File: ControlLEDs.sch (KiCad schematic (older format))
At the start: 18 parts

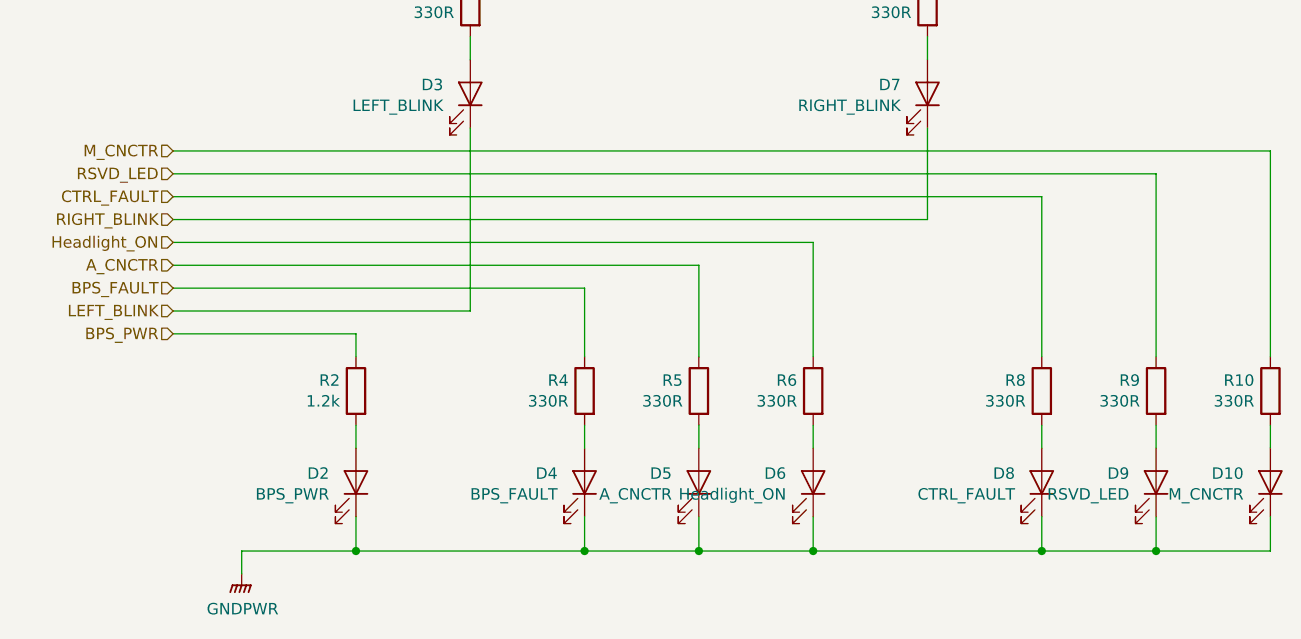
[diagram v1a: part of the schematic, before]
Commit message: Added Regen switch, deleted RSVD LED
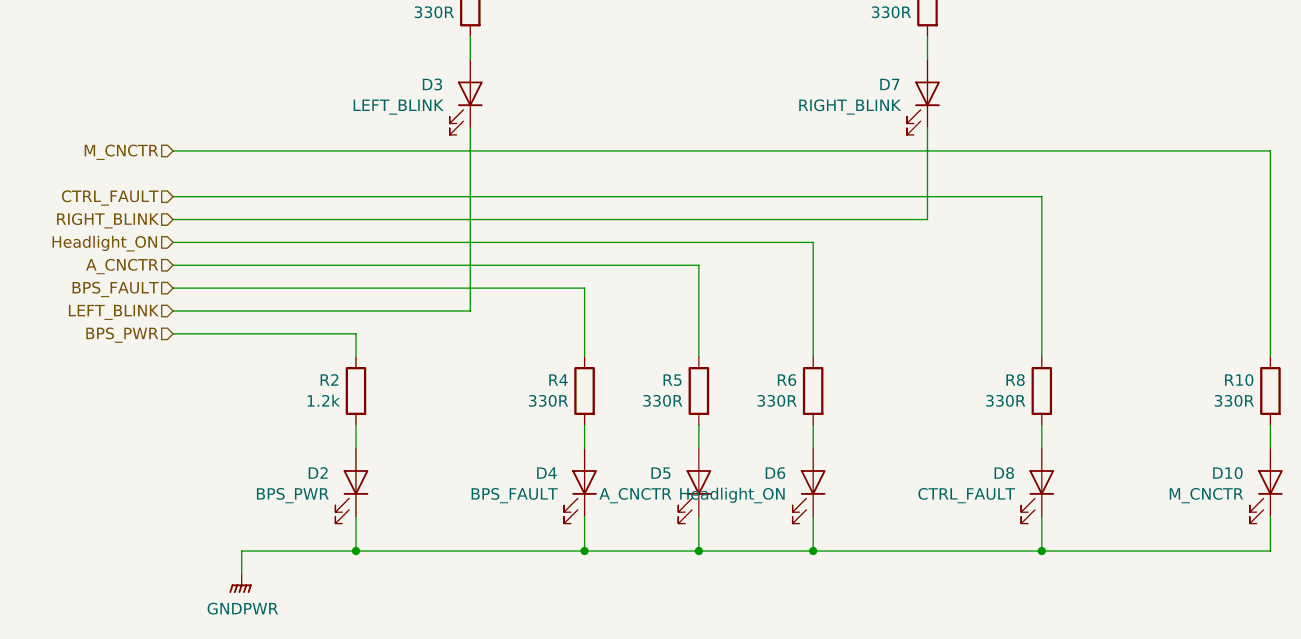
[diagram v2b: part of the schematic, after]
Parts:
- removed D9: RSVD_LED, Diode_SMD:D_0805_2012Metric, symbol Device:LED
- removed R9: 330R, Resistor_SMD:R_0805_2012Metric, symbol Device:R
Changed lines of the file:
@@
 $EndComp
-Wire Wire Line
-	7900 4250 7900 4350
 Wire Wire Line
 	7400 4250 7400 4350
@@
 Wire Wire Line
 	7400 3250 7400 3950
-Wire Wire Line
-	3600 3150 7900 3150
-Wire Wire Line
-	7900 3150 7900 3950
 Wire Wire Line
 	3600 3050 8400 3050
@@
 Wire Wire Line
 	7400 4650 7400 4800
-Wire Wire Line
-	7900 4650 7900 4800
-Wire Wire Line
-	7900 4800 7400 4800
 Connection ~ 7400 4800
 Wire Wire Line
 	8400 4650 8400 4800
-Wire Wire Line
-	8400 4800 7900 4800
-Connection ~ 7900 4800
 Wire Wire Line
 	3900 2150 3900 2050
@@
 Text HLabel 3600 3050 0    50   Input ~ 0
 M_CNCTR
-Text HLabel 3600 3150 0    50   Input ~ 0
-RSVD_LED
 Text HLabel 3600 3450 0    50   Input ~ 0
 Headlight_ON
@@
 $Comp
 L Device:R R?
-U 1 1 5F7BCB8B
-P 7900 4100
-AR Path="/5F7BCB8B" Ref="R?"  Part="1"
-AR Path="/5F7A71E1/5F7BCB8B" Ref="R9"  Part="1"
-F 0 "R9" H 7970 4146 50  0000 L CNN
-F 1 "330R" H 7970 4055 50  0000 L CNN
-F 2 "Resistor_SMD:R_0805_2012Metric" V 7830 4100 50  0001 C CNN
-F 3 "~" H 7900 4100 50  0001 C CNN
-	1    7900 4100
-	-1   0    0    -1
-$EndComp
-$Comp
-L Device:R R?
 U 1 1 5F7BCB85
 P 7400 4100
@@
 $EndComp
 $Comp
-L Device:LED D?
-U 1 1 5F7BCB61
-P 7900 4500
-AR Path="/5F7BCB61" Ref="D?"  Part="1"
-AR Path="/5F7A71E1/5F7BCB61" Ref="D9"  Part="1"
-F 0 "D9" V 7939 4383 50  0000 R CNN
-F 1 "RSVD_LED" V 7848 4383 50  0000 R CNN
-F 2 "Diode_SMD:D_0805_2012Metric" H 7900 4500 50  0001 C CNN
-F 3 "~" H 7900 4500 50  0001 C CNN
-	1    7900 4500
-	0    1    -1   0
-$EndComp
-$Comp
 L Device:R R?
 U 1 1 5F7BCB9D
@@
 	-1   0    0    -1
 $EndComp
+Wire Wire Line
+	7400 4800 8400 4800
 $EndSCHEMATC

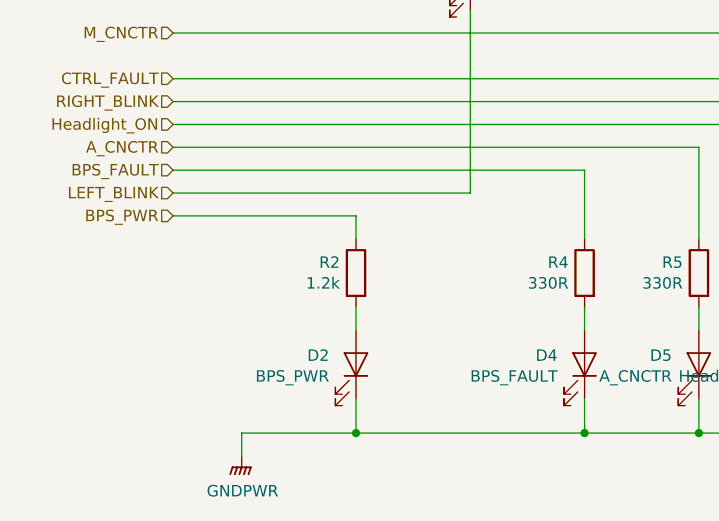
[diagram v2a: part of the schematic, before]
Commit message: Fixed BPS_PWR lines
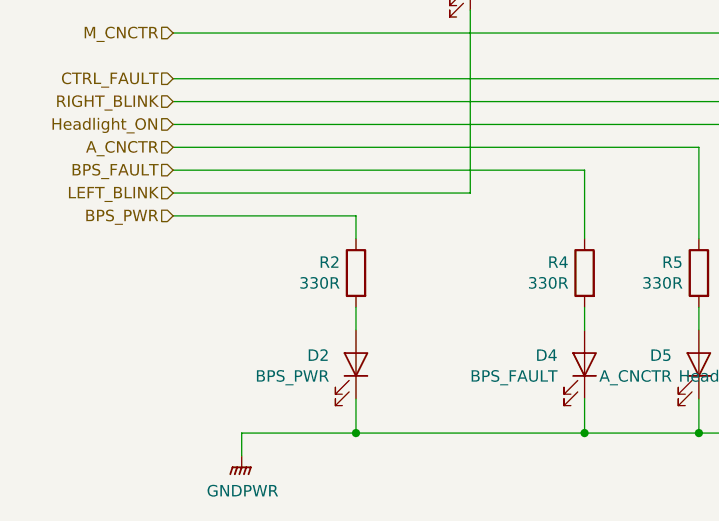
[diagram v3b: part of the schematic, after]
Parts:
- R2: value 1.2k -> 330R
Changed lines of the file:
@@
 AR Path="/5F7A71E1/5F7BCBA3" Ref="R2"  Part="1"
 F 0 "R2" H 4470 4146 50  0000 L CNN
-F 1 "1.2k" H 4470 4055 50  0000 L CNN
+F 1 "330R" H 4470 4055 50  0000 L CNN
 F 2 "Resistor_SMD:R_0805_2012Metric" V 4330 4100 50  0001 C CNN
 F 3 "~" H 4400 4100 50  0001 C CNN

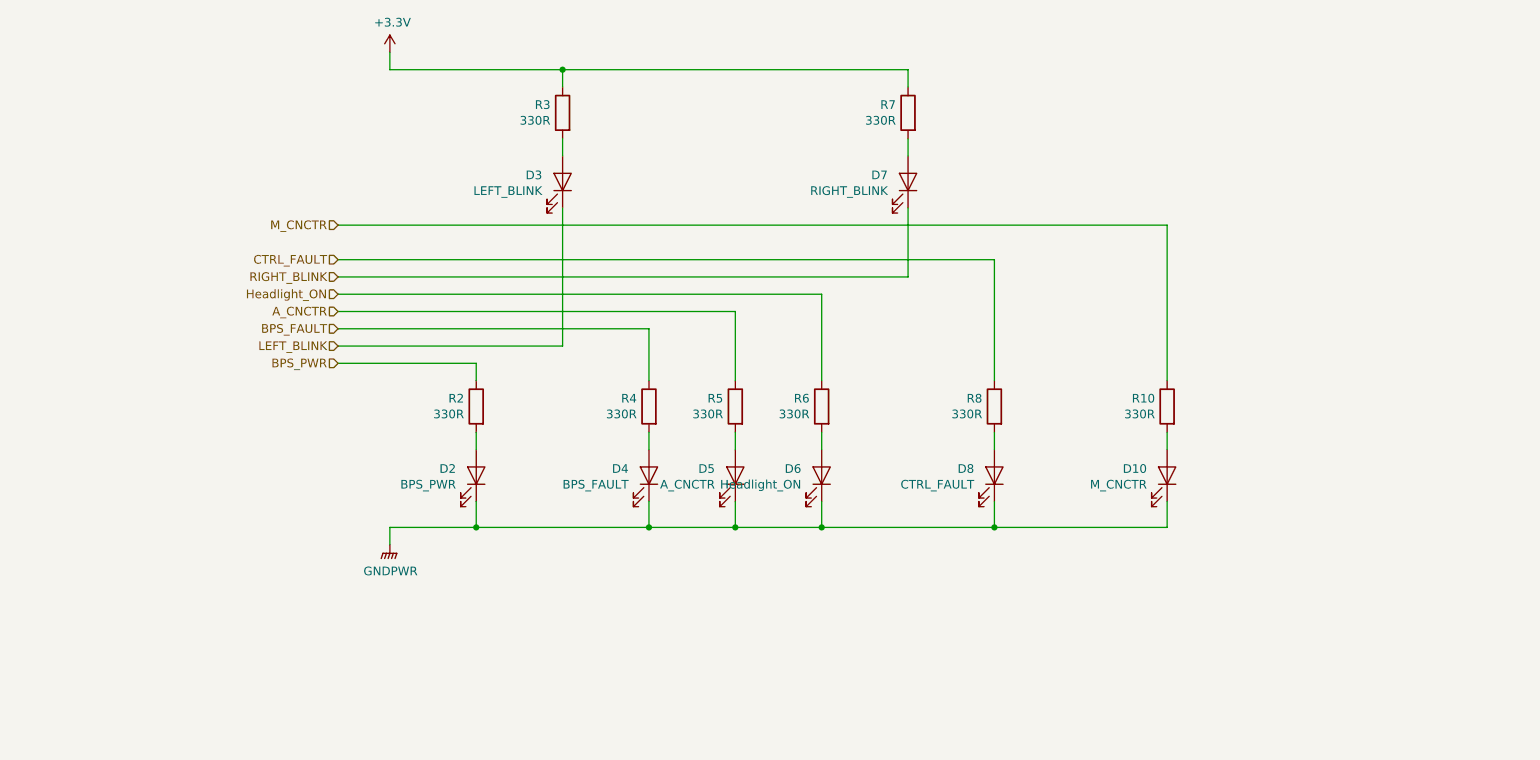
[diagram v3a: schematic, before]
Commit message: Changed Schematic, but not PCB layout. Updated LED resistor values
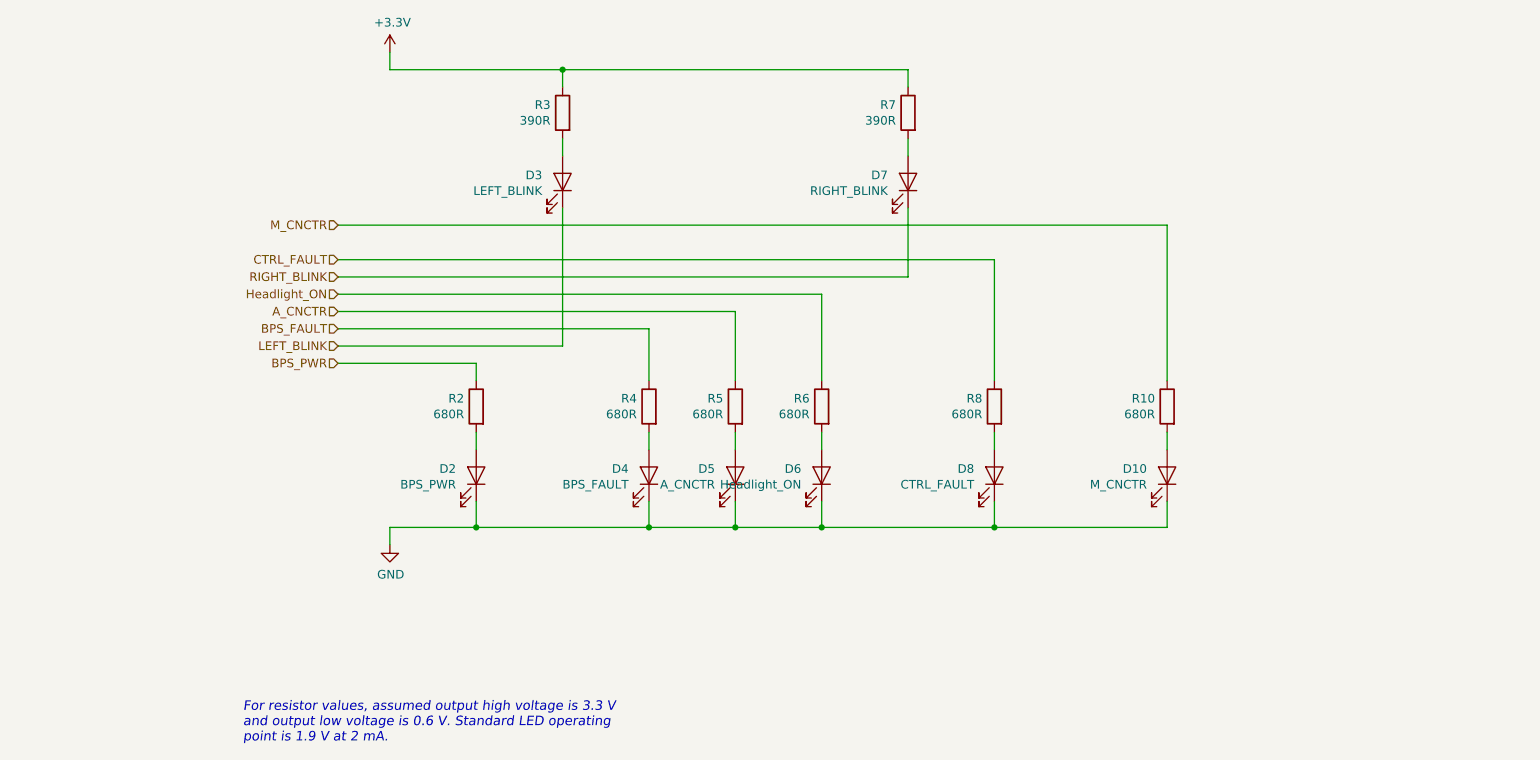
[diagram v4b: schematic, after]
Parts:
- R10, R2, R4, R5, R6, R8: value 330R -> 680R
- R3, R7: value 330R -> 390R
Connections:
- net GNDPWR renamed GND
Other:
- note added: "For resistor values, assumed output high voltage is 3.3 V \nand output low voltage is 0.6 V. Standard LED operating \npoint is 1.9 V at 2 mA."
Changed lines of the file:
@@
 $Descr A4 11693 8268
 encoding utf-8
-Sheet 2 5
+Sheet 3 4
 Title ""
 Date ""
@@
 AR Path="/5F7A71E1/5F7BCB91" Ref="R6"  Part="1"
 F 0 "R6" H 6470 4146 50  0000 L CNN
-F 1 "330R" H 6470 4055 50  0000 L CNN
+F 1 "680R" H 6470 4055 50  0000 L CNN
 F 2 "Resistor_SMD:R_0805_2012Metric" V 6330 4100 50  0001 C CNN
 F 3 "~" H 6400 4100 50  0001 C CNN
@@
 AR Path="/5F7A71E1/5F7BCBA3" Ref="R2"  Part="1"
 F 0 "R2" H 4470 4146 50  0000 L CNN
-F 1 "330R" H 4470 4055 50  0000 L CNN
+F 1 "680R" H 4470 4055 50  0000 L CNN
 F 2 "Resistor_SMD:R_0805_2012Metric" V 4330 4100 50  0001 C CNN
 F 3 "~" H 4400 4100 50  0001 C CNN
@@
 AR Path="/5F7A71E1/5F7BCBA9" Ref="R3"  Part="1"
 F 0 "R3" H 4970 2446 50  0000 L CNN
-F 1 "330R" H 4970 2355 50  0000 L CNN
+F 1 "390R" H 4970 2355 50  0000 L CNN
 F 2 "Resistor_SMD:R_0805_2012Metric" V 4830 2400 50  0001 C CNN
 F 3 "~" H 4900 2400 50  0001 C CNN
@@
 AR Path="/5F7A71E1/5F7BCBAF" Ref="R4"  Part="1"
 F 0 "R4" H 5470 4146 50  0000 L CNN
-F 1 "330R" H 5470 4055 50  0000 L CNN
+F 1 "680R" H 5470 4055 50  0000 L CNN
 F 2 "Resistor_SMD:R_0805_2012Metric" V 5330 4100 50  0001 C CNN
 F 3 "~" H 5400 4100 50  0001 C CNN
@@
 F 3 "" H 3900 2050 50  0001 C CNN
 	1    3900 2050
-	1    0    0    -1
-$EndComp
-$Comp
-L power:GNDPWR #PWR?
-U 1 1 5F7BCBC1
-P 3900 4900
-AR Path="/5F7BCBC1" Ref="#PWR?"  Part="1"
-AR Path="/5F7A71E1/5F7BCBC1" Ref="#PWR0115"  Part="1"
-F 0 "#PWR0115" H 3900 4700 50  0001 C CNN
-F 1 "GNDPWR" H 3904 4746 50  0000 C CNN
-F 2 "" H 3900 4850 50  0001 C CNN
-F 3 "" H 3900 4850 50  0001 C CNN
-	1    3900 4900
 	1    0    0    -1
 $EndComp
@@
 AR Path="/5F7A71E1/5F7BCBD8" Ref="R10"  Part="1"
 F 0 "R10" H 8470 4146 50  0000 L CNN
-F 1 "330R" H 8470 4055 50  0000 L CNN
+F 1 "680R" H 8470 4055 50  0000 L CNN
 F 2 "Resistor_SMD:R_0805_2012Metric" V 8330 4100 50  0001 C CNN
 F 3 "~" H 8400 4100 50  0001 C CNN
@@
 AR Path="/5F7A71E1/5F7BCB85" Ref="R8"  Part="1"
 F 0 "R8" H 7470 4146 50  0000 L CNN
-F 1 "330R" H 7470 4055 50  0000 L CNN
+F 1 "680R" H 7470 4055 50  0000 L CNN
 F 2 "Resistor_SMD:R_0805_2012Metric" V 7330 4100 50  0001 C CNN
 F 3 "~" H 7400 4100 50  0001 C CNN
@@
 AR Path="/5F7A71E1/5F7BCB9D" Ref="R5"  Part="1"
 F 0 "R5" H 5970 4146 50  0000 L CNN
-F 1 "330R" H 5970 4055 50  0000 L CNN
+F 1 "680R" H 5970 4055 50  0000 L CNN
 F 2 "Resistor_SMD:R_0805_2012Metric" V 5830 4100 50  0001 C CNN
 F 3 "~" H 5900 4100 50  0001 C CNN
@@
 AR Path="/5F7A71E1/5F7BCB97" Ref="R7"  Part="1"
 F 0 "R7" H 6970 2446 50  0000 L CNN
-F 1 "330R" H 6970 2355 50  0000 L CNN
+F 1 "390R" H 6970 2355 50  0000 L CNN
 F 2 "Resistor_SMD:R_0805_2012Metric" V 6830 2400 50  0001 C CNN
 F 3 "~" H 6900 2400 50  0001 C CNN
@@
 Wire Wire Line
 	7400 4800 8400 4800
+$Comp
+L power:GND #PWR020
+U 1 1 5FDE5ADE
+P 3900 4900
+F 0 "#PWR020" H 3900 4650 50  0001 C CNN
+F 1 "GND" H 3905 4727 50  0000 C CNN
+F 2 "" H 3900 4900 50  0001 C CNN
+F 3 "" H 3900 4900 50  0001 C CNN
+	1    3900 4900
+	1    0    0    -1
+$EndComp
+Text Notes 3050 6050 0    55   Italic 0
+For resistor values, assumed output high voltage is 3.3 V \nand output low voltage is 0.6 V. Standard LED operating \npoint is 1.9 V at 2 mA.
 $EndSCHEMATC

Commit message: Board finished with the new changes, needs to be checked
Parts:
- R10, R2, R5, R6, R8: value 680R -> 680
- R3, R7: value 390R -> 390
- R4: value 680R -> 5k
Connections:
- net GND: no longer D4.1 (K)
- net BPS_FAULT renamed BPS_FAULT+
- new net BPS_FAULT-: D4.1 (K)
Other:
- note added: "For all resistor values (other than BPS_FAULT), the assumed output high voltage is 3.3 V \nand output low voltage is 0.6 V. Standard LED operating point is 1.9 V at 2 mA."
- note added: "Voltage drop from BPS_FAULT+ to BPS_FAULT- \nis assumed to be 12 V."
- note removed: "For resistor values, assumed output high voltage is 3.3 V \nand output low voltage is 0.6 V. Standard LED operating \npoint is 1.9 V at 2 mA."
- moved on the sheet: D10, D2, D3, D4, D5, D6, D7, D8, R10, R2, R3, R4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

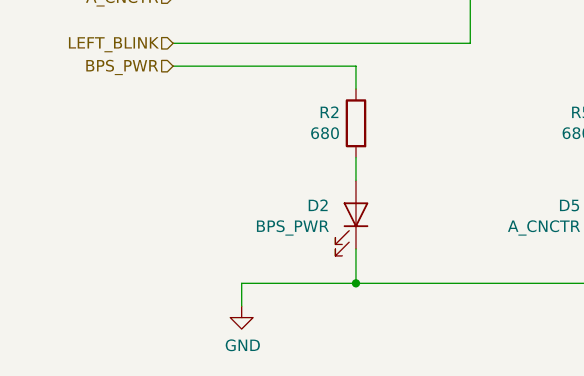
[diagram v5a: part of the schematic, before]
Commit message: isoSPI -> SPI 2
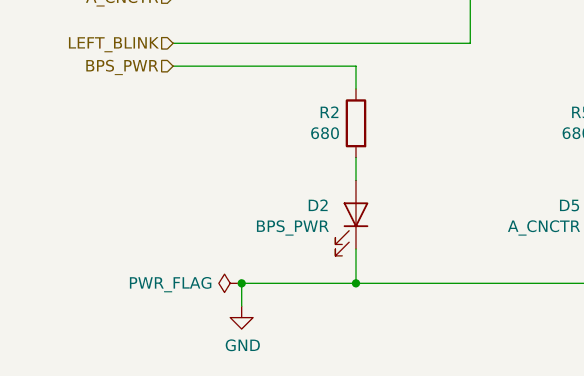
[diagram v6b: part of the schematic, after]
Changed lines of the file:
@@
 	-1   0    0    -1
 $EndComp
+$Comp
+L power:PWR_FLAG #FLG0103
+U 1 1 61A05CD3
+P 2700 5400
+F 0 "#FLG0103" H 2700 5475 50  0001 C CNN
+F 1 "PWR_FLAG" V 2700 5527 50  0000 L CNN
+F 2 "" H 2700 5400 50  0001 C CNN
+F 3 "~" H 2700 5400 50  0001 C CNN
+	1    2700 5400
+	0    -1   -1   0
+$EndComp
+Connection ~ 2700 5400
 $EndSCHEMATC
